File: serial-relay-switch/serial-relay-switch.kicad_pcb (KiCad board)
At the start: 2 copper layers, 170.2 x 66 mm, 78 parts, among them J1 Screw_Terminal_01x01, J10 Screw_Terminal_01x01, J11 Screw_Terminal_01x01, J17 Conn_01x01, J18 Conn_01x01, J19 Screw_Terminal_01x01, J2 2501551-4, J20 Screw_Terminal_01x01, J21 Conn_01x01, J4 Screw_Terminal_01x01, J5 Screw_Terminal_01x01, J6 Screw_Terminal_01x01, J7 Screw_Terminal_01x01, J8 Screw_Terminal_01x01, J9 Screw_Terminal_01x01, K1 G2RL-1-E, K2 G2RL-1-E, K3 G2RL-1-E, K4 G2RL-1-E, K5 G2RL-1-E, K6 G2RL-1-E, K7 G2RL-1-E, K8 G2RL-1-E, U1 H11L1, U10 SZNUD3124LT1G, U11 SZNUD3124LT1G, U12 SZNUD3124LT1G, U13 74HCT595, U14 74LVC1G32, U15 74LVC1G08, U16 74LVC1G04, U17 74LS163, U2 ISL8488E, U3 SZNUD3124LT1G, U4 ISL8488E, U6 SZNUD3124LT1G, U7 SZNUD3124LT1G, U8 SZNUD3124LT1G, U9 SZNUD3124LT1G

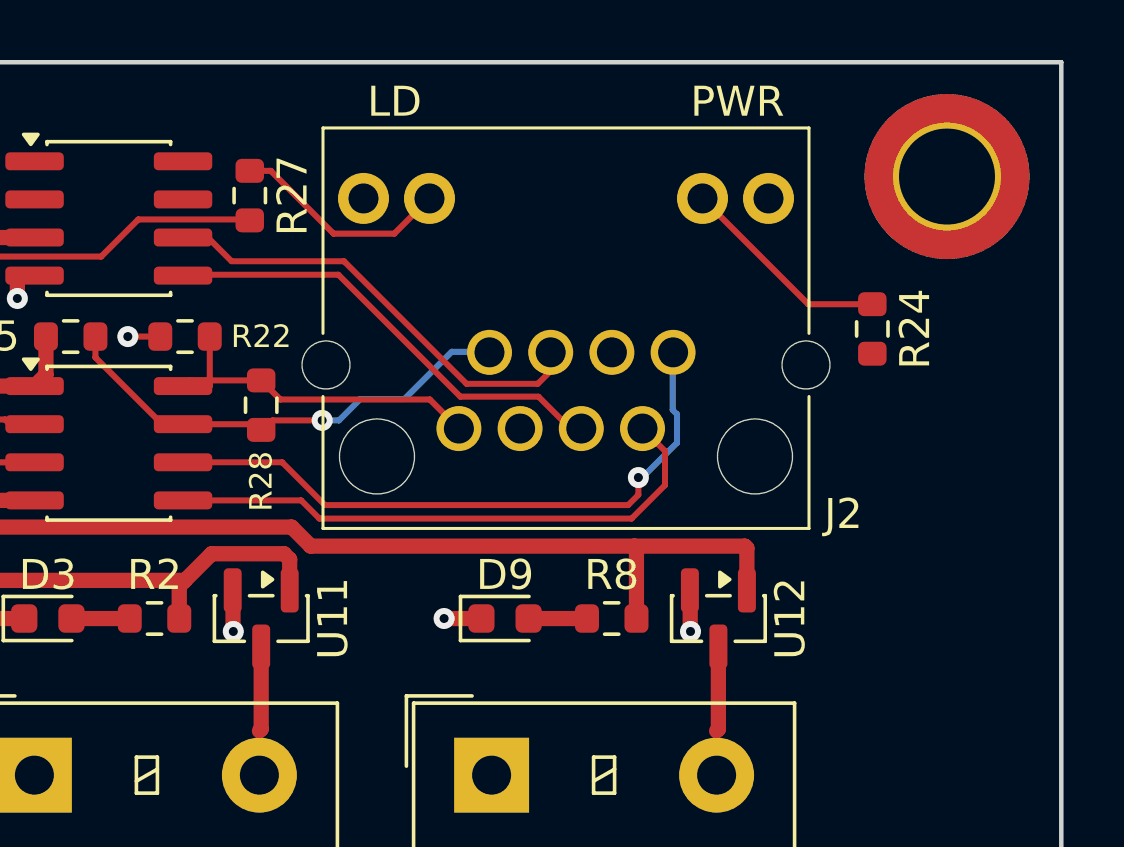
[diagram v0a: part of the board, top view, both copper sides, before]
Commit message: [rs] Add RJ-45 shield connection; Export v1.0A1 gerbers
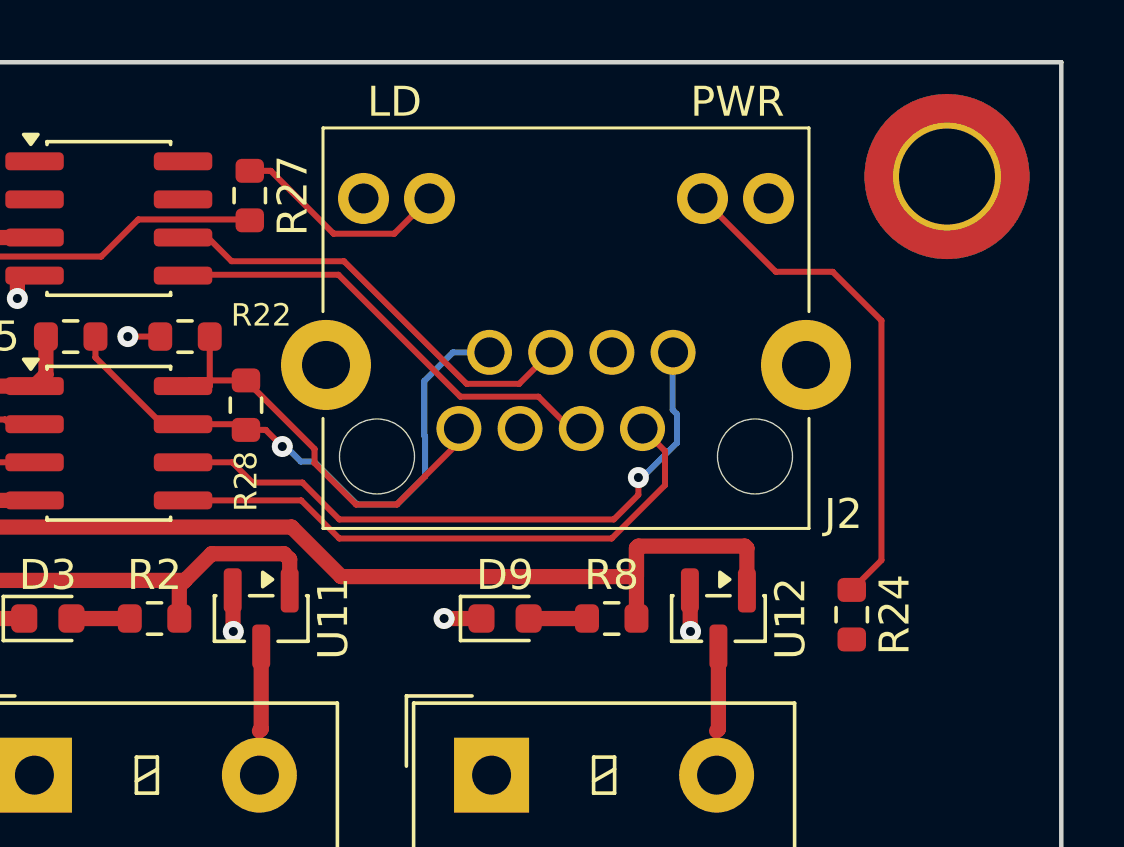
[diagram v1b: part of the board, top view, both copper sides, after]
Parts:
- moved R24 9.55 mm to (201.0, 61.0)
- moved R28 0.51 mm to (180.8, 54.0)
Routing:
- net Net-(J2-LED1+): track 7.12 -> 17.0 mm
- net /SI_N: track 15.9 -> 19.9 mm
- net /SI_P: track 12.5 -> 15.1 mm
- net /CTL_H: track 63.4 -> 64.7 mm
- net /CLK_P: track 19.0 -> 19.5 mm

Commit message: [rs] Add PoR; Change to SC-74 coil driver package
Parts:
- J1, J10, J11, J19, J20, J4, J5, J6, J7, J8, J9: footprint CUSTOM:8195 -> CUSTOM:ScrewTerminal_Keystone_8195
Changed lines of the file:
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@@
 		)
 	)
-	(footprint "CUSTOM:8195"
+	(footprint "CUSTOM:ScrewTerminal_Keystone_8195"
 		(layer "F.Cu")
 		(at 55.55 99.76)
@@
 		)
 	)
-	(footprint "CUSTOM:8195"
+	(footprint "CUSTOM:ScrewTerminal_Keystone_8195"
 		(layer "F.Cu")
 		(at 70.79 99.76)
@@
 		)
 	)
-	(footprint "CUSTOM:8195"
+	(footprint "CUSTOM:ScrewTerminal_Keystone_8195"
 		(layer "F.Cu")
 		(at 146.99 99.76)
@@
 		)
 	)
-	(footprint "CUSTOM:8195"
+	(footprint "CUSTOM:ScrewTerminal_Keystone_8195"
 		(layer "F.Cu")
 		(at 86.03 99.76)
@@
 		(embedded_fonts no)
 	)
-	(footprint "CUSTOM:8195"
+	(footprint "CUSTOM:ScrewTerminal_Keystone_8195"
 		(layer "F.Cu")
 		(at 116.51 99.76)
@@
 		(embedded_fonts no)
 	)
-	(footprint "CUSTOM:8195"
+	(footprint "CUSTOM:ScrewTerminal_Keystone_8195"
 		(layer "F.Cu")
 		(at 162.23 99.76)
@@
 		(embedded_fonts no)
 	)
-	(footprint "CUSTOM:8195"
+	(footprint "CUSTOM:ScrewTerminal_Keystone_8195"
 		(layer "F.Cu")
 		(at 131.75 99.76)
@@
 		)
 	)
-	(footprint "CUSTOM:8195"
+	(footprint "CUSTOM:ScrewTerminal_Keystone_8195"
 		(layer "F.Cu")
 		(at 44.755 56.58 -90)
@@
 		)
 	)
-	(footprint "CUSTOM:8195"
+	(footprint "CUSTOM:ScrewTerminal_Keystone_8195"
 		(layer "F.Cu")
 		(at 192.71 99.76)
@@
 		)
 	)
-	(footprint "CUSTOM:8195"
+	(footprint "CUSTOM:ScrewTerminal_Keystone_8195"
 		(layer "F.Cu")
 		(at 101.27 99.76)
@@
 		)
 	)
-	(footprint "CUSTOM:8195"
+	(footprint "CUSTOM:ScrewTerminal_Keystone_8195"
 		(layer "F.Cu")
 		(at 177.47 99.76)
@@
 			(keep_text_aligned yes)
 		)
-		(gr_text "2.3"
+		(gr_text "58.42"
 			(at 214.42 75.63 90)
 			(layer "Dwgs.User")
@@
 			(keep_text_aligned yes)
 		)
-		(gr_text "3.2"
+		(gr_text "81.28"
 			(at 163.5 31.3 0)
 			(layer "Dwgs.User")
@@
 			(keep_text_aligned yes)
 		)
-		(gr_text "0.3"
+		(gr_text "7.62"
 			(at 210.864 50.23 90)
 			(layer "Dwgs.User")
@@
 			(keep_text_aligned yes)
 		)
-		(gr_text "6.4"
+		(gr_text "162.56"
 			(at 122.86 118.168 0)
 			(layer "Dwgs.User")

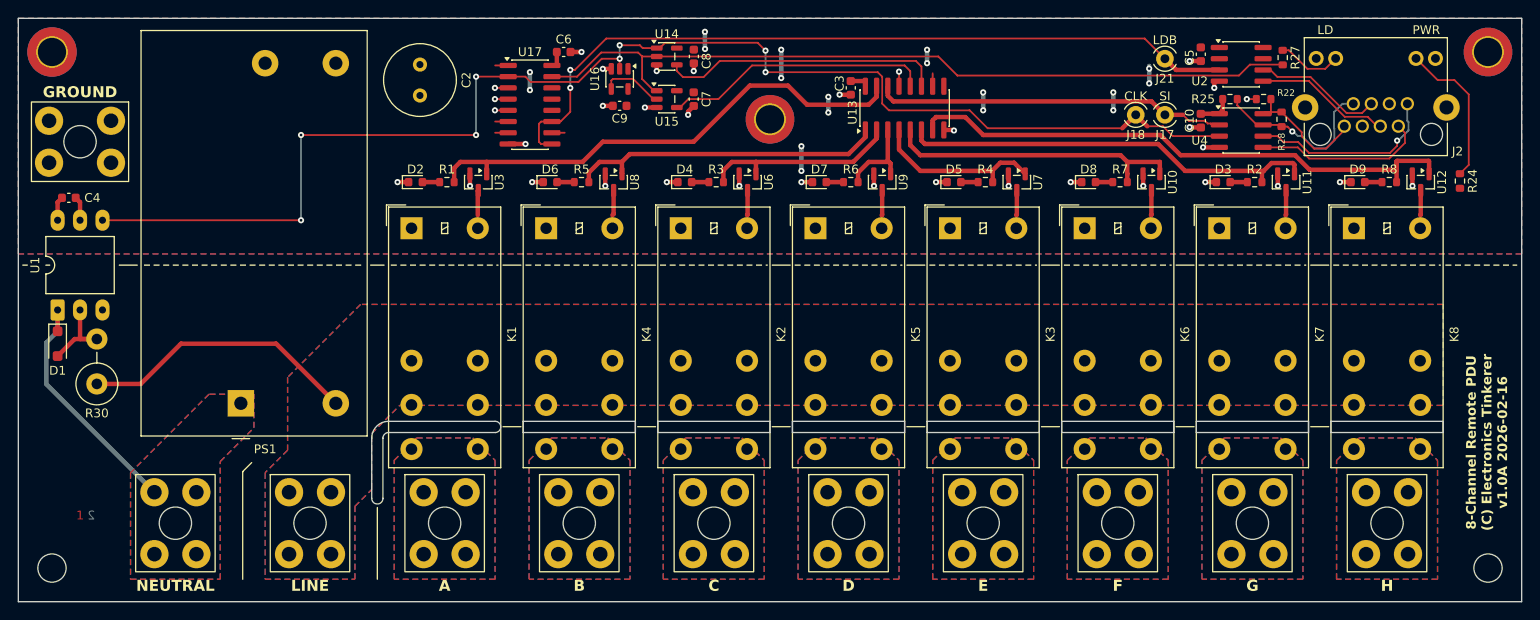
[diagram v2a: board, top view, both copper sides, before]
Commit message: [rs] Route 97cfebe + export v1.0A2 gerbers
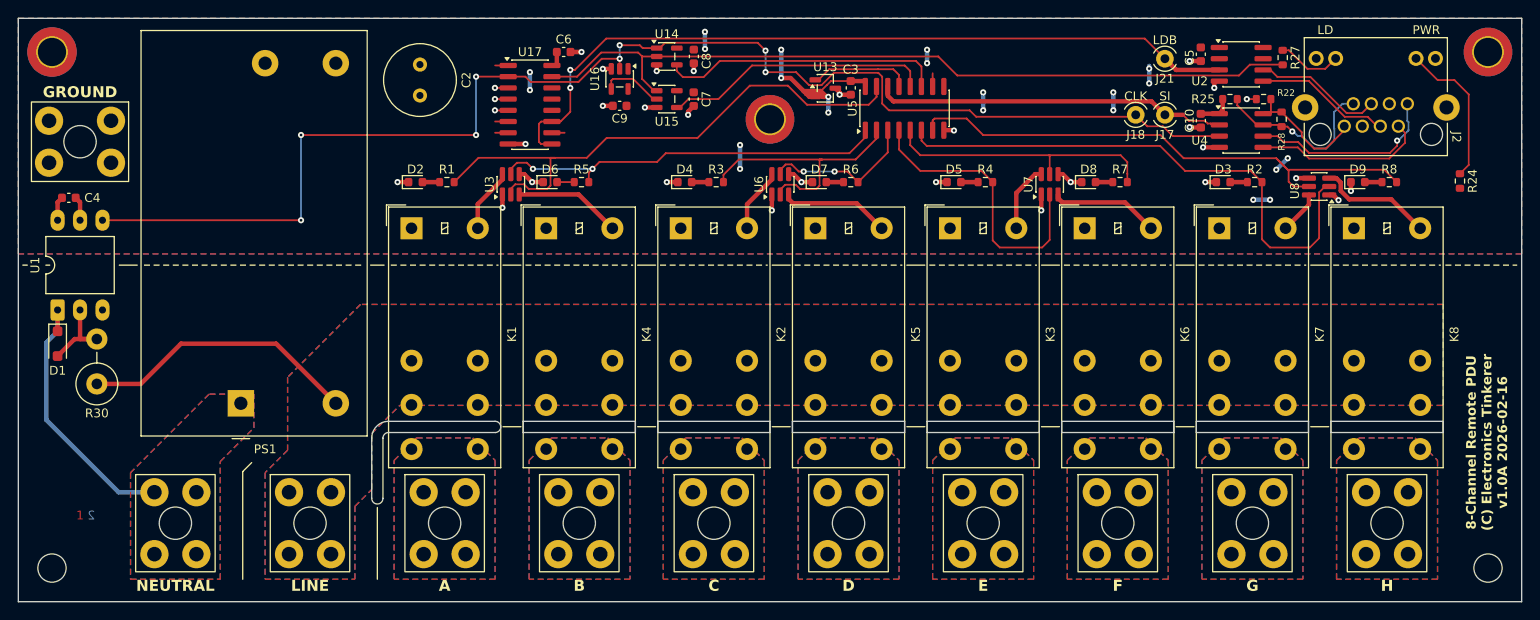
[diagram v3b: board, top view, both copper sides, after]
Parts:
- removed U10, U11, U12, U9: SZNUD3124LT1G, Package_TO_SOT_SMD:SOT-23
- added U5: 74HC594, Package_SO:SOIC-16_3.9x9.9mm_P1.27mm, F.Cu at (138.1, 52.8)
- H1, H2: footprint CUSTOM:MountingHole_3.2mm_M3 -> CUSTOM:MountingHole_3.2mm_M3_Keepout
- J2: footprint CUSTOM:2501551-4 -> CUSTOM:EthernetJack_TE_2501551-4
- U13: value 74HCT595 -> STM1810T; footprint Package_SO:SOIC-16_3.9x9.9mm_P1.27mm -> Package_TO_SOT_SMD:SOT-23-3
- U3, U6, U7, U8: value SZNUD3124LT1G -> SZNUD3124DMT1G; footprint Package_TO_SOT_SMD:SOT-23 -> Package_TO_SOT_SMD:SC-74-6_1.55x2.9mm_P0.95mm
- moved U8 79.9 mm to (185.0, 61.6), turned to 180 degrees
- moved U13 9.26 mm to (129.1, 50.5), turned to 0 degrees
- moved U7 3.73 mm to (154.5, 61.4), turned to 90 degrees
- moved U6 3.71 mm to (124.0, 61.4), turned to 90 degrees
- moved U3 3.69 mm to (93.5, 61.4), turned to 90 degrees
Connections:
- U13 pad 1: /CTL_B -> Net-(U13-RST)
- U13 pad 2: /CTL_C -> +5V
- U13 pad 3: /CTL_D -> GND
- U3 pad 1: /CTL_A -> GND
- U3 pad 2: GND -> /CTL_A
- U3 pad 3: Net-(K1-PadA2) -> Net-(K4-PadA2)
- U6 pad 1: /CTL_C -> GND
- U6 pad 2: GND -> /CTL_C
- U6 pad 3: Net-(K2-PadA2) -> Net-(K5-PadA2)
- U7 pad 1: /CTL_E -> GND
- U7 pad 2: GND -> /CTL_E
- U7 pad 3: Net-(K3-PadA2) -> Net-(K6-PadA2)
- U8 pad 1: /CTL_B -> GND
- U8 pad 2: GND -> /CTL_G
- U8 pad 3: Net-(K4-PadA2) -> Net-(K8-PadA2)
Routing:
- net +5V: track 36.9 -> 55.7 mm, vias 18 -> 22
- net /CTL_G: track 47.7 -> 62.1 mm
- net /CTL_E: track 19.7 -> 33.2 mm
- net Net-(U13-RST): track 0.00 -> 11.6 mm
- net Net-(K8-PadA2): track 2.84 -> 13.2 mm
- net Net-(K5-PadA2): track 2.84 -> 12.4 mm
- net Net-(K6-PadA2): track 2.84 -> 12.3 mm
- net Net-(K4-PadA2): track 2.87 -> 12.1 mm
- net /CTL_B: track 36.2 -> 45.3 mm, vias 0 -> 2
- net /CTL_D: track 10.4 -> 17.7 mm, vias 0 -> 2
- net /CTL_C: track 22.5 -> 29.7 mm
- net /CTL_A: track 57.1 -> 64.1 mm
- net Net-(K3-PadA2): track 2.84 -> 7.71 mm
- net Net-(K2-PadA2): track 2.84 -> 7.29 mm
- net Net-(K1-PadA2): track 2.84 -> 7.28 mm
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
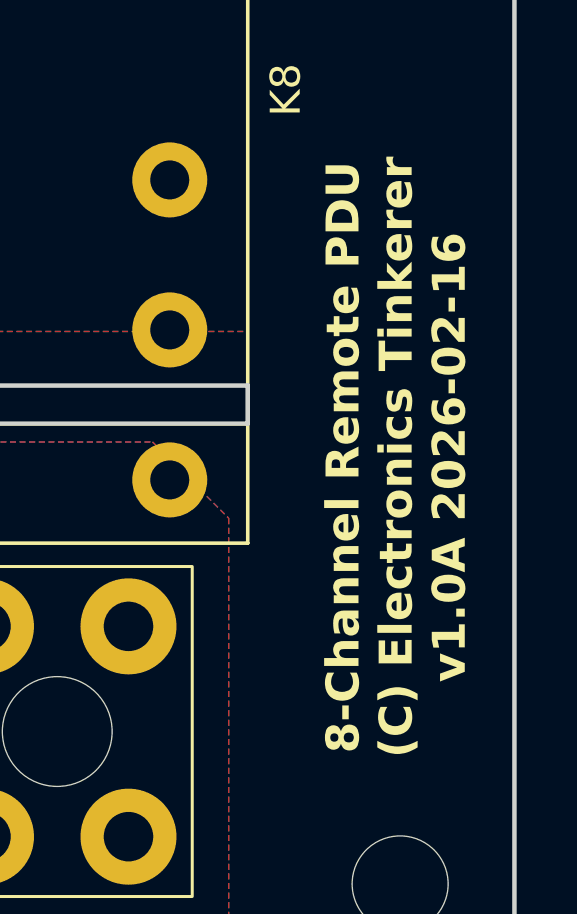
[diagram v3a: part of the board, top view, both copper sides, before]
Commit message: [rs] Update DRC rules; bump PCB to v1.0B
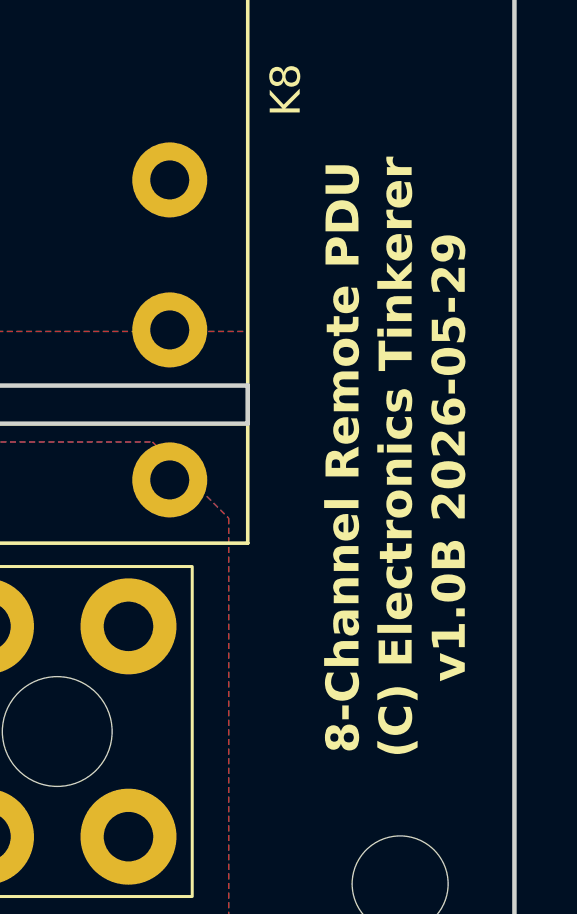
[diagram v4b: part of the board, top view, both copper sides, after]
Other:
- board text added: "8-Channel Remote PDU (C) Electronics Tinkerer v1.0B 2026-05-29"
- board text removed: "8-Channel Remote PDU (C) Electronics Tinkerer v1.0A 2026-02-16"
